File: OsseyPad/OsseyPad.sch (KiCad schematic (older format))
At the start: 90 parts, among them SW1 Rotary_Encoder_Switch, SW2 Rotary_Encoder_Switch, SW3 SW_Push, U1 ATmega32U4-MU, Y1 16MHz

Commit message: Updated the pcb.
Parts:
- removed C6, C7: 22pF, Capacitor_SMD:C_0603_1608Metric, symbol Device:C
- removed D32: PRTR5V0U2X, Package_TO_SOT_SMD:SOT-143, symbol Power_Protection:PRTR5V0U2X
- removed FB2: 50 @ 100 MHz, Inductor_SMD:L_0805_2012Metric, symbol Device:Ferrite_Bead
- removed R1, R2: 5.1k, Resistor_SMD:R_0603_1608Metric, symbol Device:R
- removed SW1: Rotary_Encoder_Switch, symbol Device:Rotary_Encoder_Switch
- removed USB1: HRO-TYPE-C-31-M-12, symbol Type-C:HRO-TYPE-C-31-M-12
- added C10, C9: 100n, Capacitor_SMD:C_0603_1608Metric, symbol Device:C_Small
- added C6, C7: 15pF, Capacitor_SMD:C_0603_1608Metric, symbol Device:C_Small
- added J1: USB_C_Receptacle_USB2.0, josh-connectors:USB_C_U262-161N-4BVC11, symbol Connector:USB_C_Receptacle_USB2.0
- added R10, R11: 5K1, Resistor_SMD:R_0603_1608Metric, symbol Device:R_Small
- added R5, R6, R7, R8, R9: 10K, Resistor_SMD:R_0603_1608Metric, symbol Device:R_Small
- added U1: USBLC6-2SC6, Package_TO_SOT_SMD:SOT-23-6, symbol Power_Protection:USBLC6-2SC6
- SW1: renamed from SW2; footprint (none) -> Rotary_Encoder:RotaryEncoder_Alps_EC11E-Switch_Vertical_H20mm_CircularMountingHoles
- SW2: renamed from SW3; footprint Button_Switch_SMD:SW_Push_1P1T_NO_6x6mm_H9.5mm -> Button_Switch_THT:SW_PUSH_6mm_H5mm
- renumbered D9 to D10, D10 to D11, D11 to D12, D12 to D13, D13 to D14, D14 to D15, D15 to D16, D16 to D17, D17 to D18, D18 to D19, D19 to D20, D20 to D21, D21 to D22, D22 to D23, D23 to D24, D24 to D25, D25 to D26, D26 to D27, D27 to D28, D28 to D29, D29 to D30, D30 to D31, D31 to D32, D5 to D6, D6 to D7, D7 to D8, D8 to D9, R5 to R1, R3 to R2, R4 to R3, R6 to R4, U1 to U2
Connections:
- net labels added: ENC_1_A, ENC_1_B, ENC_1_SW, RESET, USB_CONN_D+, USB_CONN_D-, VCC, XTAL1, XTAL2
- net labels removed: VBUS
- wire segments 251 -> 266
- no-connect marks 2 -> 14
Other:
- moved on the sheet: C1, C2, C3, C4, C5, C8, H1, H2, H3, H4, R1, R2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

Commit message: Updatet the pcb and added first versio off the firmware.
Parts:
- removed R9: 10K, Resistor_SMD:R_0603_1608Metric, symbol Device:R_Small
- added D5: 1N4148W, Diode_SMD:D_SOD-123, symbol Diode:1N4148
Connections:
- net +5V: no longer SW1.S1
- net COL5: now also SW1.S1
- net D+: no longer R2.1, U2.4 (D+)
- net D-: no longer R3.1, U2.3 (D-)
- net ROW0: now also D5.1 (K)
- net ENC_1_SW: no longer names the net of SW1.S2
- net ENC_1_SW: now also D5.2 (A); no longer U2.20 (PD2)
- new net D_Filt_+: R2.1, U2.4 (D+)
- new net D_Filt_-: R3.1, U2.3 (D-)
- no-connect marks 14 -> 15
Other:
- note added: "Switch matrix and rotary encoder"
- note removed: "Switch matrix\n"
- moved on the sheet: C10, C9, D1, D10, D11, D12, D13, D14, D15, D16, D17, D18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

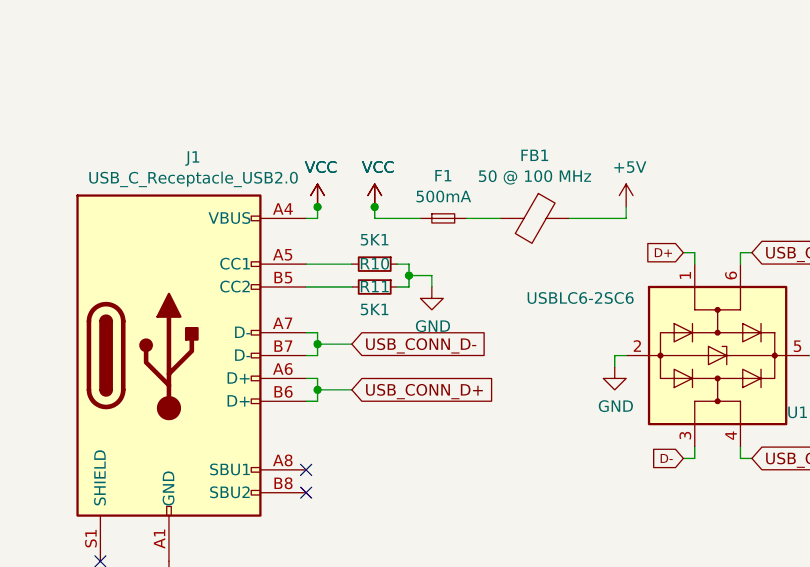
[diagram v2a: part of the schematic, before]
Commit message: Updatet the pcb and added models for the case.
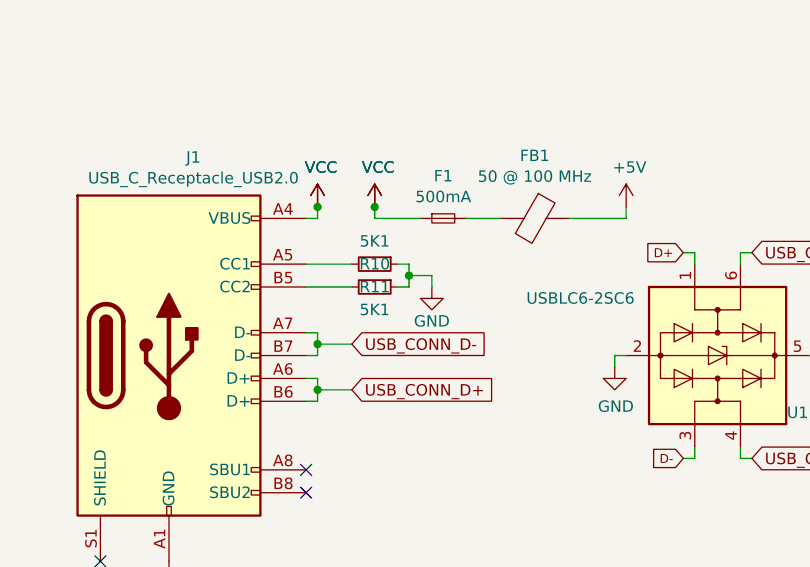
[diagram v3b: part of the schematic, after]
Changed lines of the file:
@@
 P 7350 1700
 F 0 "R10" V 7350 1700 50  0000 C CNN
-F 1 "5K1" V 7245 1700 50  0000 C CNN
+F 1 "5K1" V 7250 1700 50  0000 C CNN
 F 2 "Resistor_SMD:R_0603_1608Metric" H 7350 1700 50  0001 C CNN
 F 3 "~" H 7350 1700 50  0001 C CNN
@@
 P 7600 1800
 F 0 "#PWR024" H 7600 1550 50  0001 C CNN
-F 1 "GND" H 7605 1627 50  0000 C CNN
+F 1 "GND" H 7600 1650 50  0000 C CNN
 F 2 "" H 7600 1800 50  0001 C CNN
 F 3 "" H 7600 1800 50  0001 C CNN
@@
 	8400 2100 8400 2150
 $Comp
-L Hello_to_horse:LOGO #G1
+L OsseyPad-rescue:LOGO-Hello_to_horse #G1
 U 1 1 5FF49842
 P 11050 10350

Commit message: PCB Update.
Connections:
- net GND: no longer C1.2, C2.2, C3.2, C4.2, C5.2
- new net: C1.2, C2.2, C3.2, C4.2, C5.2
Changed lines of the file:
@@
 L power:+5V #PWR02
 U 1 1 6025B469
-P 13750 1600
-F 0 "#PWR02" H 13750 1450 50  0001 C CNN
-F 1 "+5V" H 13765 1773 50  0000 C CNN
-F 2 "" H 13750 1600 50  0001 C CNN
-F 3 "" H 13750 1600 50  0001 C CNN
-	1    13750 1600
+P 13750 1500
+F 0 "#PWR02" H 13750 1350 50  0001 C CNN
+F 1 "+5V" H 13765 1673 50  0000 C CNN
+F 2 "" H 13750 1500 50  0001 C CNN
+F 3 "" H 13750 1500 50  0001 C CNN
+	1    13750 1500
 	1    0    0    -1
 $EndComp
@@
 L power:GND #PWR07
 U 1 1 6025C816
-P 13750 2100
-F 0 "#PWR07" H 13750 1850 50  0001 C CNN
-F 1 "GND" H 13755 1927 50  0000 C CNN
-F 2 "" H 13750 2100 50  0001 C CNN
-F 3 "" H 13750 2100 50  0001 C CNN
-	1    13750 2100
+P 13750 2200
+F 0 "#PWR07" H 13750 1950 50  0001 C CNN
+F 1 "GND" H 13755 2027 50  0000 C CNN
+F 2 "" H 13750 2200 50  0001 C CNN
+F 3 "" H 13750 2200 50  0001 C CNN
+	1    13750 2200
 	1    0    0    -1
 $EndComp
@@
 	0    1    1    0
 $EndComp
-Wire Wire Line
-	13350 5100 13250 5100
 $Comp
 L power:GND #PWR015
@@
 Wire Wire Line
 	14550 5900 14750 5900
-Wire Wire Line
-	13850 7100 13900 7100
-Wire Wire Line
-	13900 7100 13900 7350
-Connection ~ 13900 7100
-Wire Wire Line
-	13900 7100 13950 7100
 $Comp
 L power:GND #PWR017
@@
 	12350 3950 12050 3950
 Connection ~ 12050 3950
-Connection ~ 13750 1600
-Connection ~ 13750 2100
-Wire Wire Line
-	13850 3350 13850 3200
-Connection ~ 13850 3350
+Wire Wire Line
+	13950 3350 13950 3200
 $Comp
 L power:+5V #PWR011
 U 1 1 6016228A
-P 13850 3200
-F 0 "#PWR011" H 13850 3050 50  0001 C CNN
-F 1 "+5V" H 13865 3373 50  0000 C CNN
-F 2 "" H 13850 3200 50  0001 C CNN
-F 3 "" H 13850 3200 50  0001 C CNN
-	1    13850 3200
+P 13950 3200
+F 0 "#PWR011" H 13950 3050 50  0001 C CNN
+F 1 "+5V" H 13965 3373 50  0000 C CNN
+F 2 "" H 13950 3200 50  0001 C CNN
+F 3 "" H 13950 3200 50  0001 C CNN
+	1    13950 3200
 	1    0    0    -1
 $EndComp
@@
 	1    0    0    -1
 $EndComp
-$Comp
-L MCU_Microchip_ATmega:ATmega32U4-MU U2
-U 1 1 5FEF5B5B
-P 13950 5300
-F 0 "U2" H 14450 7050 50  0000 C CNN
-F 1 "ATmega32U4-MU" H 14400 3500 50  0000 C CNN
-F 2 "Package_DFN_QFN:QFN-44-1EP_7x7mm_P0.5mm_EP5.2x5.2mm" H 13950 5300 50  0001 C CIN
-F 3 "http://ww1.microchip.com/downloads/en/DeviceDoc/Atmel-7766-8-bit-AVR-ATmega16U4-32U4_Datasheet.pdf" H 13950 5300 50  0001 C CNN
-	1    13950 5300
-	1    0    0    -1
-$EndComp
-Wire Wire Line
-	13350 4600 12950 4600
 Wire Wire Line
 	12950 4600 12950 4500
@@
 	1    0    0    -1
 $EndComp
+Wire Wire Line
+	13750 1600 13750 1500
+Connection ~ 13750 1600
+Wire Wire Line
+	13350 5100 13250 5100
+Wire Wire Line
+	13350 4600 12950 4600
+$Comp
+L MCU_Microchip_ATmega:ATmega32U4-MU U2
+U 1 1 5FEF5B5B
+P 13950 5300
+F 0 "U2" H 14450 7050 50  0000 C CNN
+F 1 "ATmega32U4-MU" H 14400 3500 50  0000 C CNN
+F 2 "Package_DFN_QFN:QFN-44-1EP_7x7mm_P0.5mm_EP5.2x5.2mm" H 13950 5300 50  0001 C CIN
+F 3 "http://ww1.microchip.com/downloads/en/DeviceDoc/Atmel-7766-8-bit-AVR-ATmega16U4-32U4_Datasheet.pdf" H 13950 5300 50  0001 C CNN
+	1    13950 5300
+	1    0    0    -1
+$EndComp
+Wire Wire Line
+	13850 7100 13850 7150
+Wire Wire Line
+	13950 7150 13950 7100
+Wire Wire Line
+	13850 7150 13900 7150
+Wire Wire Line
+	13900 7150 13900 7350
+Connection ~ 13900 7150
+Wire Wire Line
+	13900 7150 13950 7150
 $EndSCHEMATC
